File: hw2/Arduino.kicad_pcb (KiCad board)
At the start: 2 copper layers, 28 parts, among them P1 CONN_01X02, P2 CONN_01X12, P3 CONN_01X12, P4 USB-A-PCB, U1 MIC5219, U2 ATmega32U4

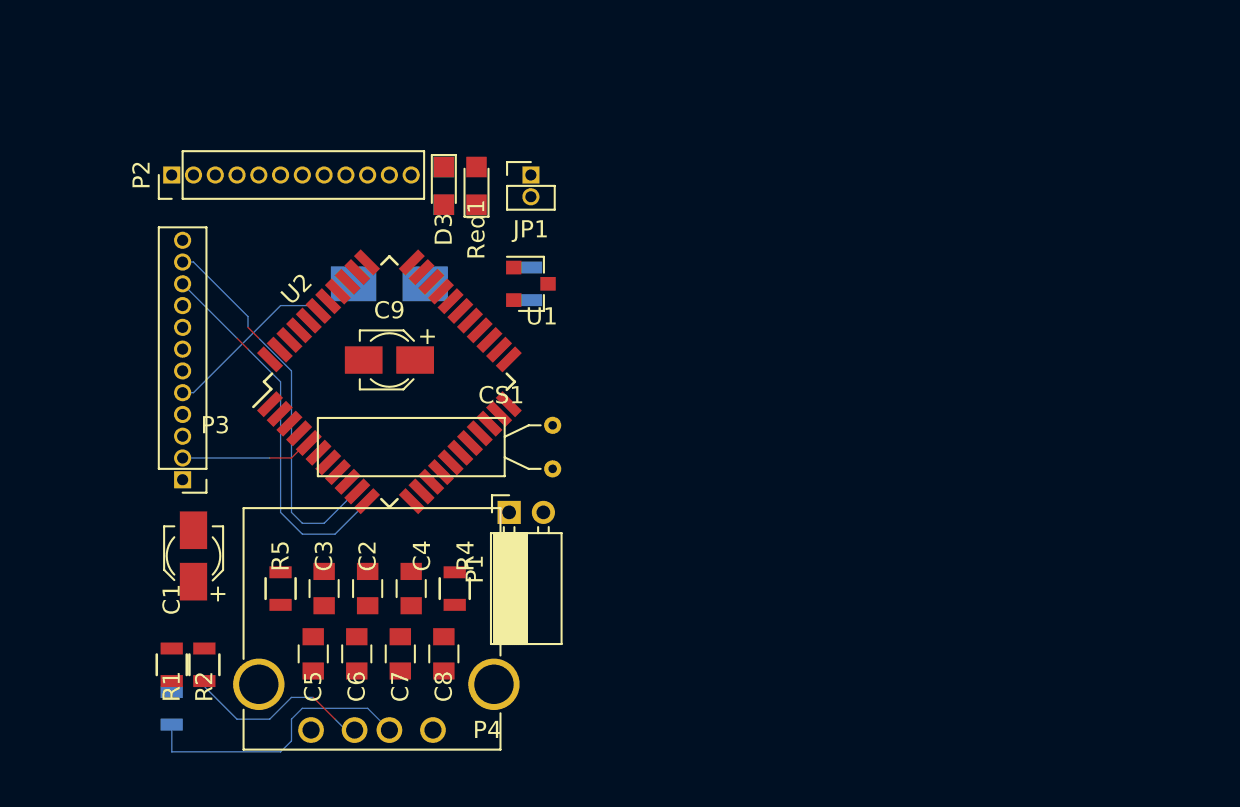
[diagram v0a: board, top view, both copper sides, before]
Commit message: Main elements repositioned
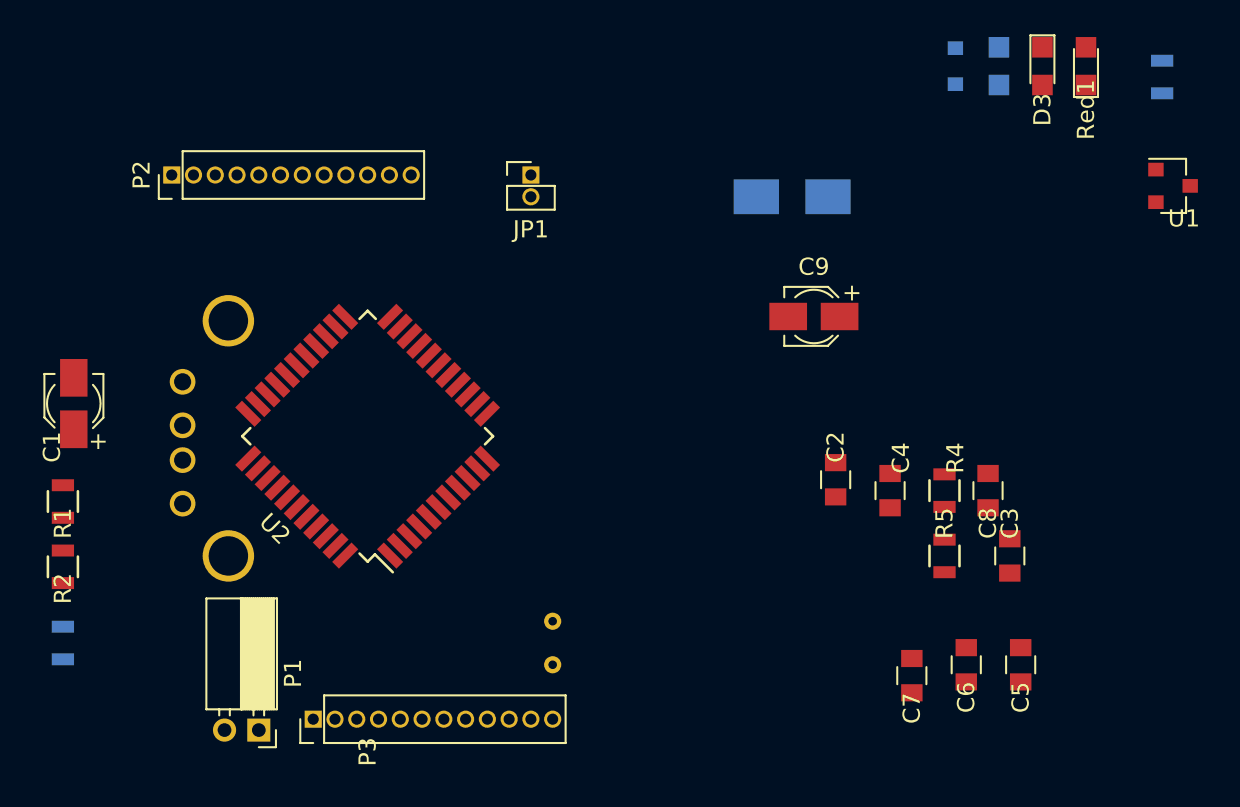
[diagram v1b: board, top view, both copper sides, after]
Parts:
- CS1, P4: moved to B.Cu
- moved C5 41.3 mm to (120.0, 72.4)
- moved C3 40.1 mm to (119.4, 66.0)
- moved R5 38.8 mm to (115.6, 66.0)
- moved R6 38.8 mm to (128.3, 38.1)
- moved U1 37.9 mm to (128.9, 44.5)
- moved Red1 36.2 mm to (123.8, 37.5)
- moved D3 35.6 mm to (121.3, 37.5)
- moved C6 35.6 mm to (116.8, 72.4)
- moved C8 33.1 mm to (118.1, 62.2)
- moved D2 33.1 mm to (118.7, 37.5)
- moved C7 29.9 mm to (113.7, 73.0)
- moved R4 29.1 mm to (115.6, 62.2)
- moved D1 28.8 mm to (116.2, 37.5)
- moved C4 28.5 mm to (112.4, 62.2)
- moved C2 28.0 mm to (109.2, 61.6)
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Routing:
- net /MOSI: track 22.5 -> 0.00 mm, vias 2 -> 0
- net /MISO: track 22.1 -> 0.00 mm, vias 2 -> 0
- net Net-(P4-Pad2): track 16.6 -> 0.00 mm
- net Net-(P4-Pad3): track 10.9 -> 0.00 mm, vias 2 -> 0
- net /A3: track 9.72 -> 0.00 mm
- net GND: track 7.72 -> 0.00 mm, vias 1 -> 0

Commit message: Advances in pcblayout
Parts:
- C2, P1, R5, U1: moved to B.Cu
- R6: moved to F.Cu
- moved D2 43.2 mm to (86.4, 66.0), turned to 0 degrees
- moved U1 42.7 mm to (87.0, 52.7), turned to 180 degrees
- moved D3 33.3 mm to (99.7, 62.9), turned to 180 degrees
- moved R5 29.3 mm to (86.4, 63.5), turned to 180 degrees
- moved D1 29.1 mm to (91.4, 52.7)
- moved C2 25.3 mm to (87.0, 49.5), turned to 0 degrees
- moved Fuse1 24.8 mm to (85.7, 58.4), turned to 90 degrees
- moved R6 20.4 mm to (111.8, 50.2), turned to 0 degrees
- moved C9 17.9 mm to (91.4, 45.1), turned to 270 degrees
- moved JP1 4.49 mm to (87.0, 43.2)
- moved P1 1.42 mm to (74.3, 75.6)
- moved P4 0.64 mm to (71.1, 55.2)
- moved U2 0.63 mm to (81.9, 58.4)

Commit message: Tracks initialized
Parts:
- C3, R1: moved to B.Cu
- moved Red1 38.0 mm to (87.0, 47.0), turned to 180 degrees
- moved C3 36.7 mm to (90.2, 43.8), turned to 270 degrees
- moved R1 31.6 mm to (91.4, 47.0), turned to 180 degrees
- moved Fuse1 28.5 mm to (113.7, 52.7)
- moved R5 23.3 mm to (108.0, 54.6)
- moved D2 19.8 mm to (106.0, 64.1)
- moved U1 14.2 mm to (101.0, 55.2)
- moved D1 10.3 mm to (101.6, 50.8)
- moved R4 9.61 mm to (125.1, 61.0)
- moved C2 8.08 mm to (92.7, 43.8), turned to 270 degrees
- moved R6 7.65 mm to (111.1, 42.5)
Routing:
- net GND: track 0.00 -> 36.4 mm, vias 0 -> 1
- net /D9: track 0.00 -> 19.0 mm, vias 0 -> 3
- net /D8: track 0.00 -> 17.1 mm, vias 0 -> 3
- net /D3: track 0.00 -> 15.3 mm, vias 0 -> 1
- net /D5: track 0.00 -> 14.9 mm, vias 0 -> 3
- net /D2: track 0.00 -> 14.2 mm, vias 0 -> 1
- net /D6: track 0.00 -> 11.9 mm, vias 0 -> 1
- net VCC: track 0.00 -> 11.2 mm, vias 0 -> 3
- net /RXI: track 0.00 -> 9.99 mm, vias 0 -> 2
- net /D4: track 0.00 -> 9.99 mm, vias 0 -> 1
- net Net-(R1-Pad2): track 0.00 -> 8.53 mm, vias 0 -> 1
- net /TX0: track 0.00 -> 8.48 mm

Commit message: Routing finalized
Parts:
- C4, C5, C8, D3, R2, R4, R6: moved to B.Cu
- D1, Fuse1, U1: moved to F.Cu
- moved C6 41.5 mm to (75.6, 68.6), turned to 0 degrees
- moved R4 38.3 mm to (87.0, 57.1), turned to 315 degrees
- moved C5 33.3 mm to (87.0, 67.9), turned to 180 degrees
- moved Fuse1 31.9 mm to (87.1, 70.4), turned to 270 degrees
- moved R6 30.6 mm to (82.8, 54.1), turned to 315 degrees
- moved C8 27.1 mm to (91.1, 63.0), turned to 180 degrees
- moved D1 26.6 mm to (84.5, 71.1)
- moved U1 24.8 mm to (81.9, 71.1), turned to 90 degrees
- moved C7 23.8 mm to (89.9, 71.6)
- moved C4 22.8 mm to (90.2, 67.3)
- moved R5 22.7 mm to (85.9, 59.9), turned to 45 degrees
- moved D2 22.6 mm to (84.1, 58.9), turned to 45 degrees
- moved D3 19.8 mm to (81.3, 55.6), turned to 135 degrees
- moved R3 19.7 mm to (78.5, 57.7), turned to 135 degrees
- moved C1 19.4 mm to (77.5, 71.8), turned to 180 degrees
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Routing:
- net GND: track 36.4 -> 142.4 mm, vias 1 -> 11
- net VCC: track 11.2 -> 108.0 mm, vias 3 -> 14
- net /D10: track 0.00 -> 50.5 mm, vias 0 -> 2
- net Net-(D1-Pad2): track 0.00 -> 45.5 mm, vias 0 -> 2
- net /SCK: track 0.00 -> 33.3 mm, vias 0 -> 3
- net /D7: track 0.00 -> 33.2 mm, vias 0 -> 2
- net Net-(C7-Pad1): track 0.00 -> 30.3 mm, vias 0 -> 1
- net /A0: track 0.00 -> 21.9 mm, vias 0 -> 1
- net /MISO: track 0.00 -> 21.6 mm, vias 0 -> 2
- net Net-(C8-Pad1): track 0.00 -> 19.5 mm, vias 0 -> 1
- net /A1: track 0.00 -> 19.1 mm, vias 0 -> 3
- net /A2: track 0.00 -> 18.7 mm, vias 0 -> 3
- net /A3: track 0.00 -> 16.8 mm, vias 0 -> 1
- net /MOSI: track 0.00 -> 16.6 mm, vias 0 -> 2
- net /UVCC: track 0.00 -> 13.8 mm, vias 0 -> 1
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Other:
- board outline added: 24.8 x 35.6 mm

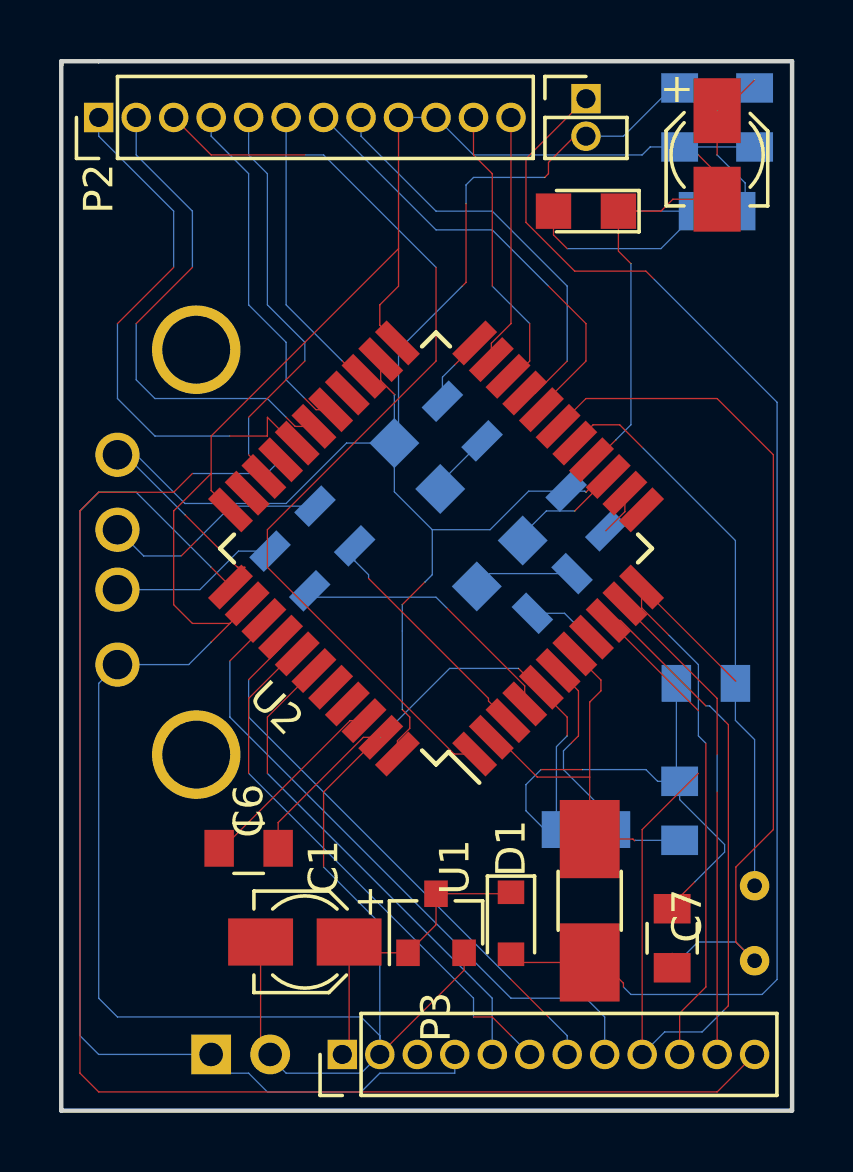
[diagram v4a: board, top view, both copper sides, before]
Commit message: USB footprint correctd; routing updated; report updated
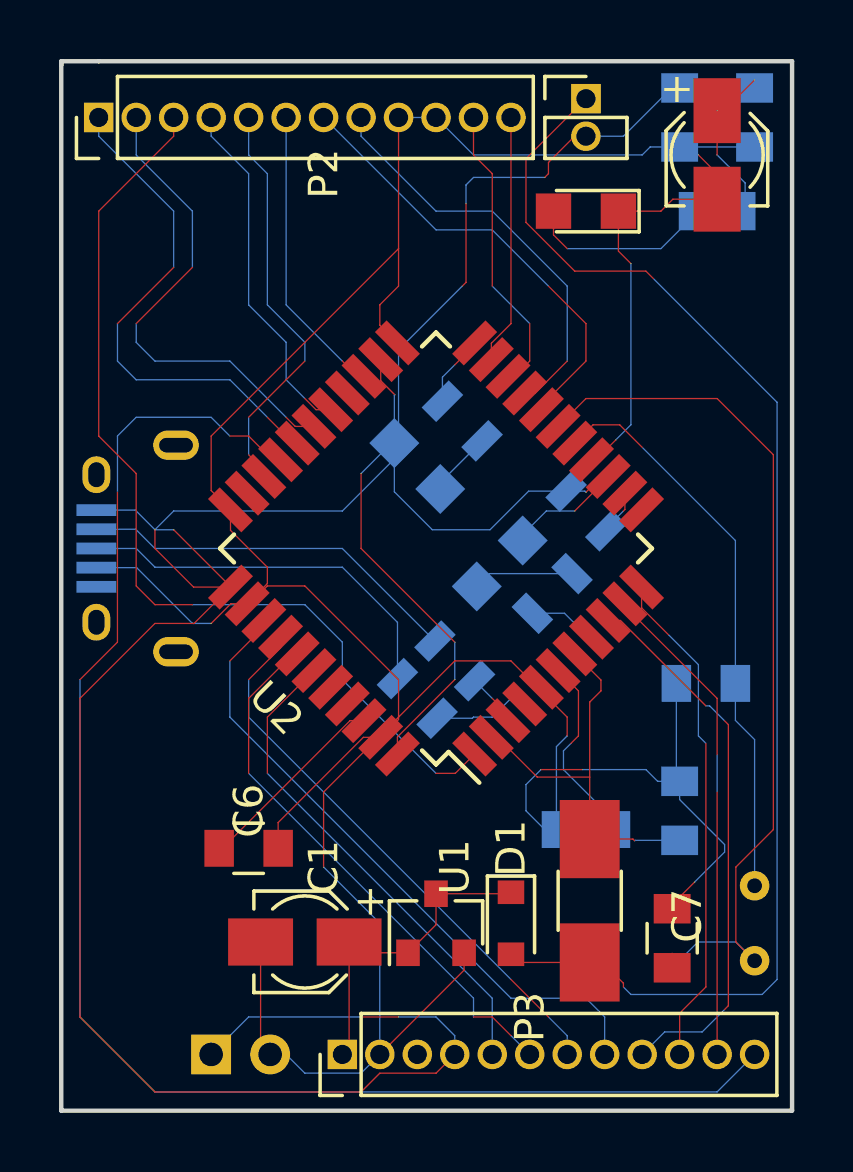
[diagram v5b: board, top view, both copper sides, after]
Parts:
- P4: footprint Connectors:USB_A -> Connectors:USB_Micro-B
- moved R3 6.12 mm to (82.5, 62.2)
- moved R2 6.11 mm to (81.3, 63.5)
- moved P4 3.24 mm to (71.8, 58.4)
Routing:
- net GND: track 142.4 -> 127.1 mm, vias 11 -> 9
- net /SCK: track 33.3 -> 18.7 mm
- net VCC: track 108.0 -> 117.8 mm, vias 14 -> 16
- net Net-(P4-Pad3): track 5.71 -> 13.1 mm
- net /D-: track 8.08 -> 1.82 mm
- net /D+: track 9.23 -> 3.32 mm
- net Net-(P4-Pad2): track 7.76 -> 13.0 mm, vias 2 -> 0
- net /MISO: track 21.6 -> 17.1 mm
- net Net-(R1-Pad2): track 8.53 -> 6.30 mm
- net /D9: track 19.0 -> 17.3 mm
- net /D8: track 17.1 -> 16.4 mm
- net /D7: track 33.2 -> 32.6 mm
- net /D10: track 50.5 -> 51.0 mm, vias 2 -> 3
- net Net-(R4-Pad2): vias 1 -> 2
- net (no net): vias 1 -> 0
